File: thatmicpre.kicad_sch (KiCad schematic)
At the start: 81 parts

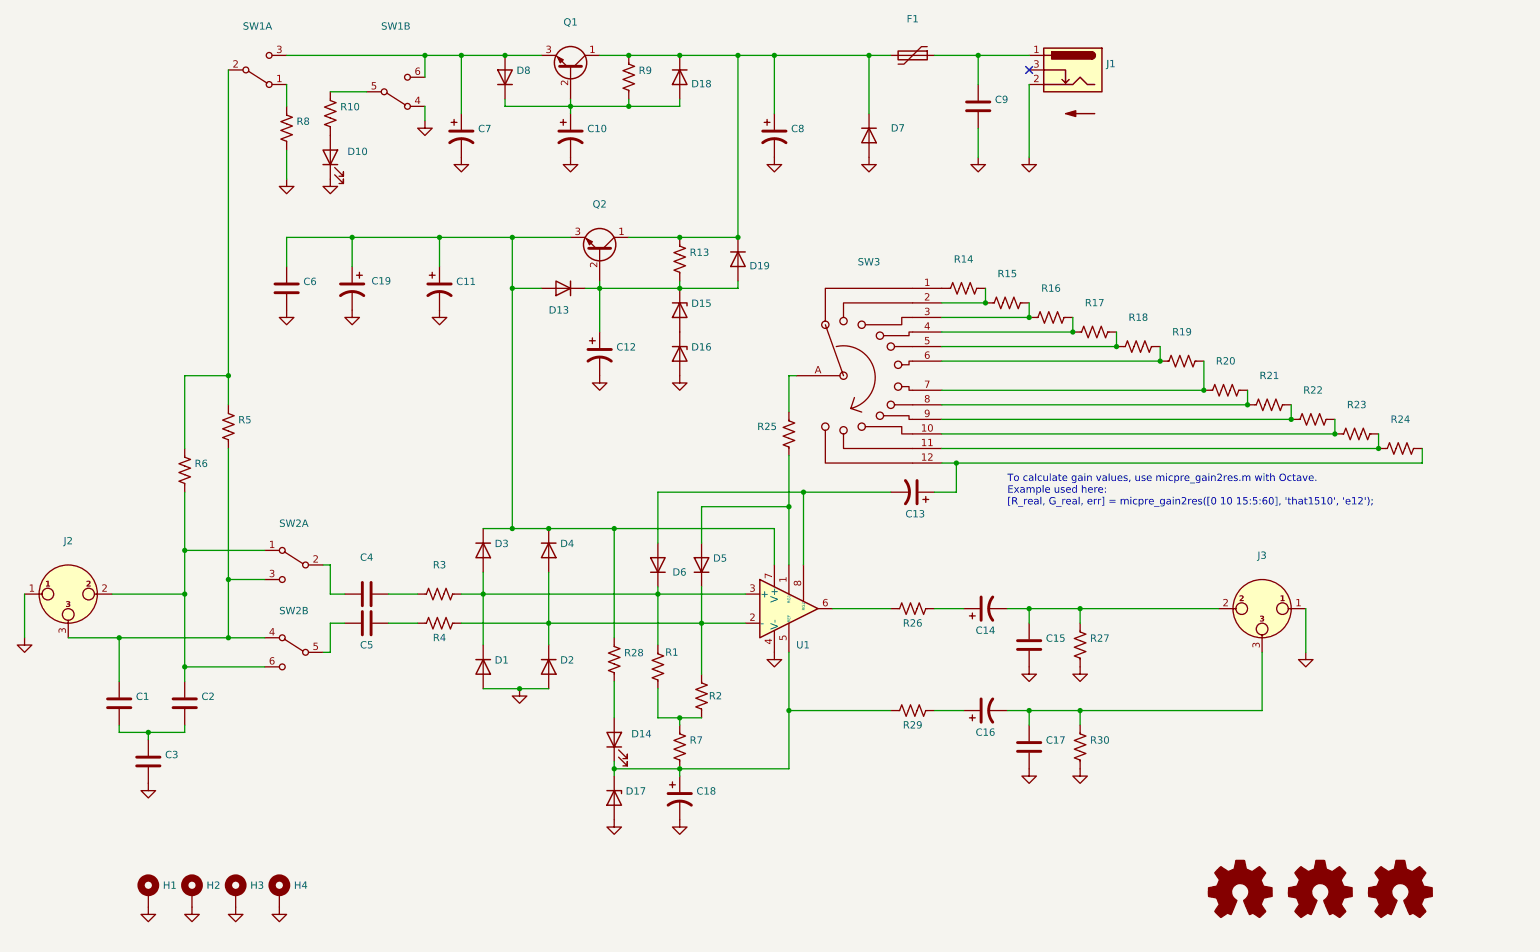
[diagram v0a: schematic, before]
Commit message: Replace csv bom with InteractiveHtmlBom
Update mfr part nr for some resistors and capacitors,
to more affordable and easily obtained parts.
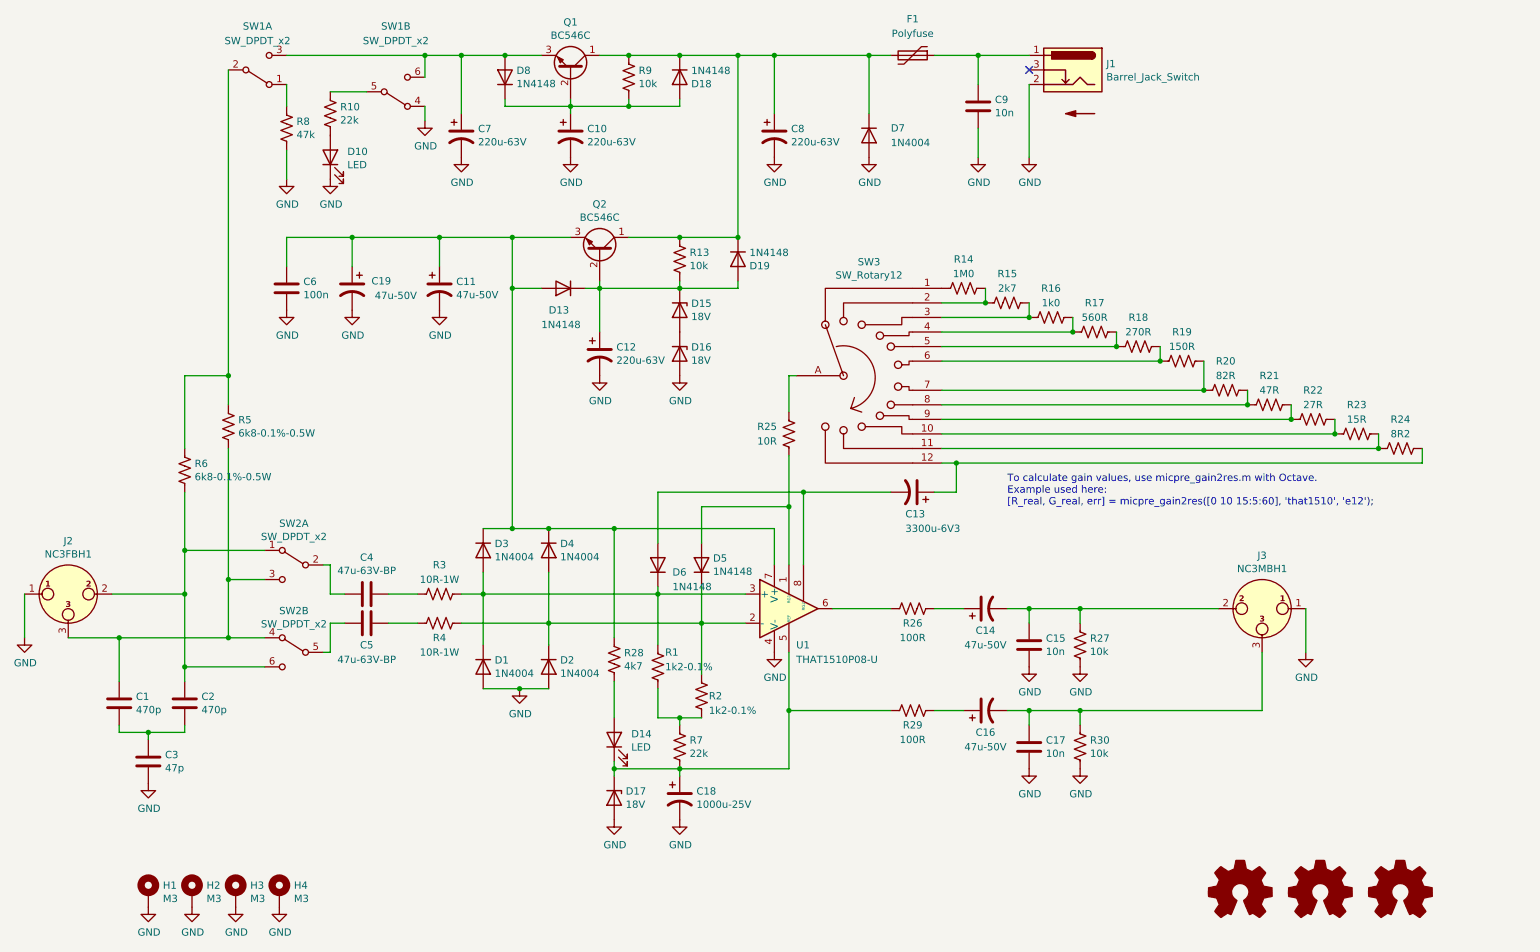
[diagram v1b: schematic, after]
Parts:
- C1, C2: value (none) -> 470p; footprint (none) -> Capacitor_THT:C_Disc_D5.0mm_W2.5mm_P5.00mm; Mfr Part Nr (none) -> RDE5C2A471J0M1H03A; Vendor RDE5C2A471J0M1H03A -> (none)
- C10, C12, C7, C8: value (none) -> 220u-63V; footprint (none) -> Capacitor_THT:CP_Radial_D10.0mm_P5.00mm; Mfr Part Nr (none) -> UVZ1J221MPD; Vendor UPW1J221MPD -> (none)
- C11, C14, C16, C19: value (none) -> 47u-50V; footprint (none) -> Capacitor_THT:CP_Radial_D6.3mm_P2.50mm; Mfr Part Nr (none) -> UFW1H470MED1TD; Vendor UFW1H470MED1TD -> (none)
- C13: value (none) -> 3300u-6V3; footprint (none) -> Capacitor_THT:CP_Radial_D10.0mm_P5.00mm; Mfr Part Nr (none) -> UFW0J332MPD; Vendor UFW0J332MPD -> (none)
- C15, C17, C9: value (none) -> 10n; footprint (none) -> Capacitor_THT:C_Rect_L7.2mm_W3.0mm_P5.00mm_FKS2_FKP2_MKS2_MKP2; Mfr Part Nr (none) -> PHE426DJ5100JR05; Vendor PHE426DJ5100JR05 -> (none)
- C18: value (none) -> 1000u-25V; footprint (none) -> Capacitor_THT:CP_Radial_D10.0mm_P5.00mm; Mfr Part Nr (none) -> UVZ1E102MPD1CM; Vendor UVZ1E102MPD1CM -> (none)
- C3: value (none) -> 47p; footprint (none) -> Capacitor_THT:C_Disc_D5.0mm_W2.5mm_P5.00mm; Mfr Part Nr (none) -> RDE5C2A470J0M1H03A; Vendor RDE5C2A470J0M1H03A -> (none)
- C4, C5: value (none) -> 47u-63V-BP; footprint (none) -> Capacitor_THT:C_Radial_D10.0mm_H16.0mm_P5.00mm; Mfr Part Nr (none) -> UEP1J470MPD; Vendor UVP1J470MPD -> (none)
- C6: value (none) -> 100n; footprint (none) -> Capacitor_THT:C_Rect_L7.2mm_W3.0mm_P5.00mm_FKS2_FKP2_MKS2_MKP2; Mfr Part Nr (none) -> R82EC3100AA70J; Vendor R82EC3100AA70J -> (none)
- D1, D2, D3, D4, D7: value (none) -> 1N4004; footprint (none) -> Diode_THT:D_DO-41_SOD81_P10.16mm_Horizontal; Mfr Part Nr (none) -> 1N4004GP-E3/54; Vendor 1N4004GP-E3/54 -> (none)
- D10, D14: value (none) -> LED; footprint (none) -> LED_THT:LED_D3.0mm; Mfr Part Nr (none) -> LTL-4232N; Vendor LTL-4232N -> (none)
- D13, D18, D19, D5, D6, D8: value (none) -> 1N4148; footprint (none) -> Diode_THT:D_DO-34_SOD68_P7.62mm_Horizontal; Mfr Part Nr (none) -> 1N4148; Vendor 1N4148 -> (none)
- D15, D16, D17: value (none) -> 18V; footprint (none) -> Diode_THT:D_DO-34_SOD68_P7.62mm_Horizontal; Mfr Part Nr (none) -> BZX55B18-TAP; Vendor BZX55B18-TAP -> (none)
- F1: value (none) -> Polyfuse; footprint (none) -> Fuse:Fuse_BelFuse_0ZRE0005FF_L8.3mm_W3.8mm; Mfr Part Nr (none) -> 0ZRC0015FF1E; Vendor 0ZRC0015FF1E -> (none)
- H1, H2, H3, H4: value (none) -> M3; footprint (none) -> MountingHole:MountingHole_3.2mm_M3_Pad
- J1: value (none) -> Barrel_Jack_Switch; footprint (none) -> Connector_BarrelJack:BarrelJack_Horizontal; Mfr Part Nr (none) -> CON-SOCJ-2155; Vendor CON-SOCJ-2155 -> (none)
- J2: value (none) -> NC3FBH1; footprint (none) -> my_kicad_footprints:Jack_XLR_Neutrik_NC3FBH1_Horizontal; Mfr Part Nr (none) -> NC3FBH1; Vendor NC3FBH1 -> (none)
- J3: value (none) -> NC3MBH1; footprint (none) -> my_kicad_footprints:Jack_XLR_Neutrik_NC3MBH_Horizontal; Mfr Part Nr (none) -> NC3MBH; Vendor NC3MBH -> (none)
- LOGO1: value (none) -> Logo_Open_Hardware_Small; footprint (none) -> Symbol:OSHW-Symbol_6.7x6mm_Copper
- LOGO2: value (none) -> Logo_Open_Hardware_Small; footprint (none) -> Symbol:Symbol_CC-Attribution_CopperTop_Small
- LOGO3: value (none) -> Logo_Open_Hardware_Small; footprint (none) -> Symbol:Symbol_CreativeCommons_CopperTop_Type2_Small
- LOGO4: value (none) -> SYM_Arrow_Normal; footprint (none) -> Symbol:Symbol_Barrel_Polarity
- Q1, Q2: value (none) -> BC546C; footprint (none) -> Package_TO_SOT_THT:TO-92_Inline_Wide; Mfr Part Nr (none) -> BC546CTA; Vendor BC546CTA -> (none)
- R1, R2: value (none) -> 1k2-0.1%; footprint (none) -> Resistor_THT:R_Axial_DIN0207_L6.3mm_D2.5mm_P10.16mm_Horizontal; Mfr Part Nr (none) -> YR1B1K21CC; Vendor YR1B1K21CC -> (none)
- R10, R7: value (none) -> 22k; footprint (none) -> Resistor_THT:R_Axial_DIN0207_L6.3mm_D2.5mm_P10.16mm_Horizontal; Mfr Part Nr (none) -> MF0207FTE52-22K; Vendor MBB02070C2202FCT00 -> (none)
- R13, R27, R30, R9: value (none) -> 10k; footprint (none) -> Resistor_THT:R_Axial_DIN0207_L6.3mm_D2.5mm_P10.16mm_Horizontal; Mfr Part Nr (none) -> MF0207FTE52-10K; Vendor MBB02070C1002FCT00 -> (none)
- R14: value (none) -> 1M0; footprint (none) -> Resistor_THT:R_Axial_DIN0207_L6.3mm_D2.5mm_P10.16mm_Horizontal; Mfr Part Nr (none) -> MF0207FTE52-1M; Vendor MBB02070C1004FCT00 -> (none)
- R15: value (none) -> 2k7; footprint (none) -> Resistor_THT:R_Axial_DIN0207_L6.3mm_D2.5mm_P10.16mm_Horizontal; Mfr Part Nr (none) -> MF0207FRE52-2K7; Vendor MBB02070C2701FC100 -> (none)
- R16: value (none) -> 1k0; footprint (none) -> Resistor_THT:R_Axial_DIN0207_L6.3mm_D2.5mm_P10.16mm_Horizontal; Mfr Part Nr (none) -> MF0207FRE52-1K; Vendor MBB02070C1001FC100 -> (none)
- R17: value (none) -> 560R; footprint (none) -> Resistor_THT:R_Axial_DIN0207_L6.3mm_D2.5mm_P10.16mm_Horizontal; Mfr Part Nr (none) -> MF0207FTE52-560R; Vendor MBB02070C5600FC100 -> (none)
- R18: value (none) -> 270R; footprint (none) -> Resistor_THT:R_Axial_DIN0207_L6.3mm_D2.5mm_P10.16mm_Horizontal; Mfr Part Nr (none) -> MF0207FTE52-270R; Vendor MBB02070C2700FC100 -> (none)
- R19: value (none) -> 150R; footprint (none) -> Resistor_THT:R_Axial_DIN0207_L6.3mm_D2.5mm_P10.16mm_Horizontal; Mfr Part Nr (none) -> MF0207FTE52-150R; Vendor MBB02070C1500FC100 -> (none)
- R20: value (none) -> 82R; footprint (none) -> Resistor_THT:R_Axial_DIN0207_L6.3mm_D2.5mm_P10.16mm_Horizontal; Mfr Part Nr (none) -> MF0207FTE52-82R; Vendor MFR50SFTE52-82R -> (none)
- R21: value (none) -> 47R; footprint (none) -> Resistor_THT:R_Axial_DIN0207_L6.3mm_D2.5mm_P10.16mm_Horizontal; Mfr Part Nr (none) -> MF0207FTE52-47R; Vendor MFR50SFTE52-47R -> (none)
- R22: value (none) -> 27R; footprint (none) -> Resistor_THT:R_Axial_DIN0207_L6.3mm_D2.5mm_P10.16mm_Horizontal; Mfr Part Nr (none) -> MF0207FTE52-27R; Vendor MFR50SFTE52-27R -> (none)
- R23: value (none) -> 15R; footprint (none) -> Resistor_THT:R_Axial_DIN0207_L6.3mm_D2.5mm_P10.16mm_Horizontal; Mfr Part Nr (none) -> MF0207FTE52-15R; Vendor MFR50SFTE52-15R -> (none)
- R24: value (none) -> 8R2; footprint (none) -> Resistor_THT:R_Axial_DIN0207_L6.3mm_D2.5mm_P10.16mm_Horizontal; Mfr Part Nr (none) -> MF0207FTE52-8R2; Vendor MFR50SFTE52-8R2 -> (none)
- R25: value (none) -> 10R; footprint (none) -> Resistor_THT:R_Axial_DIN0207_L6.3mm_D2.5mm_P10.16mm_Horizontal; Mfr Part Nr (none) -> MF0207FTE52-10R; Vendor CPF110R000BHE14 -> (none)
- R26, R29: value (none) -> 100R; footprint (none) -> Resistor_THT:R_Axial_DIN0207_L6.3mm_D2.5mm_P10.16mm_Horizontal; Mfr Part Nr (none) -> MF0207FTE52-100R; Vendor MFR50SFTE52-100R -> (none)
- R28: value (none) -> 4k7; footprint (none) -> Resistor_THT:R_Axial_DIN0207_L6.3mm_D2.5mm_P10.16mm_Horizontal; Mfr Part Nr (none) -> MF0207FRE52-4K7; Vendor MBB02070C4701FCT00 -> (none)
- R3, R4: value (none) -> 10R-1W; footprint (none) -> Resistor_THT:R_Axial_DIN0207_L6.3mm_D2.5mm_P10.16mm_Horizontal; Mfr Part Nr (none) -> CPF110R000FKEE6; Vendor CPF110R000FEB14 -> (none)
- R5, R6: value (none) -> 6k8-0.1%-0.5W; footprint (none) -> Resistor_THT:R_Axial_DIN0207_L6.3mm_D2.5mm_P10.16mm_Horizontal; Mfr Part Nr (none) -> CMF556K8100BEEK; Vendor CMF556K8100BEEK -> (none)
- R8: value (none) -> 47k; footprint (none) -> Resistor_THT:R_Axial_DIN0207_L6.3mm_D2.5mm_P10.16mm_Horizontal; Mfr Part Nr (none) -> MF0207FTE52-47K; Vendor MBB02070C4702FCT00 -> (none)
- SW1, SW2: value (none) -> SW_DPDT_x2; footprint (none) -> Button_Switch_THT:SW_Push_2P2T_Vertical_E-Switch_800UDP8P1A1M6; Mfr Part Nr (none) -> 200MDP1T2B2M6QE; Vendor 200MDP1T2B2M6QE -> (none)
- SW3: value (none) -> SW_Rotary12; footprint (none) -> my_kicad_footprints:LORINCK1049; Mfr Part Nr (none) -> SR2612F-0112-38F5B-D8-S; Vendor SR2612F-0112-38F5B-D8-S -> (none)
- U1: value (none) -> THAT1510P08-U; footprint (none) -> Package_DIP:DIP-8_W7.62mm; Mfr Part Nr (none) -> 1510P08-U; Vendor THAT1510P08-U -> (none)
